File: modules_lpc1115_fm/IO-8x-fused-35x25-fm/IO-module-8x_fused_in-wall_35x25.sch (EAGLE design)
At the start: 82 parts, among them IC1 LPC1115, IC2 ATAES132A-SHEQ-T, Q2 ASFL, U1 EEPROM, X3 MICROMATCH-10

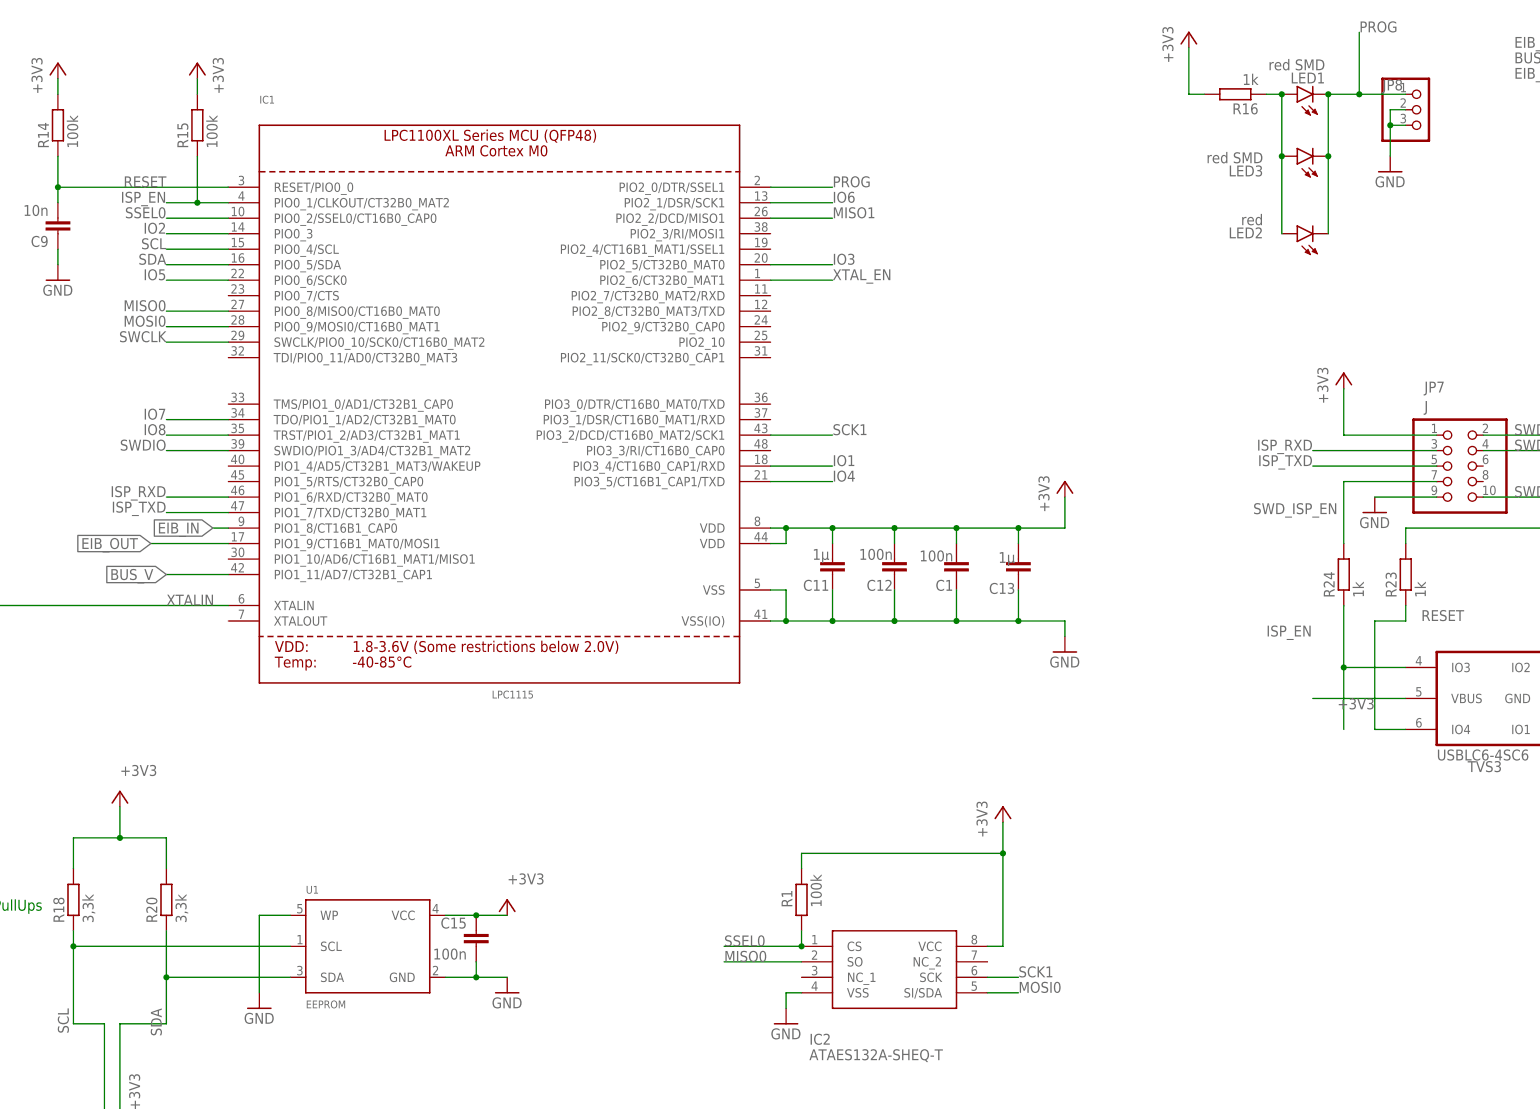
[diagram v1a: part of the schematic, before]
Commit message: [IOmodule8xUP] fixed errors with SPI routing
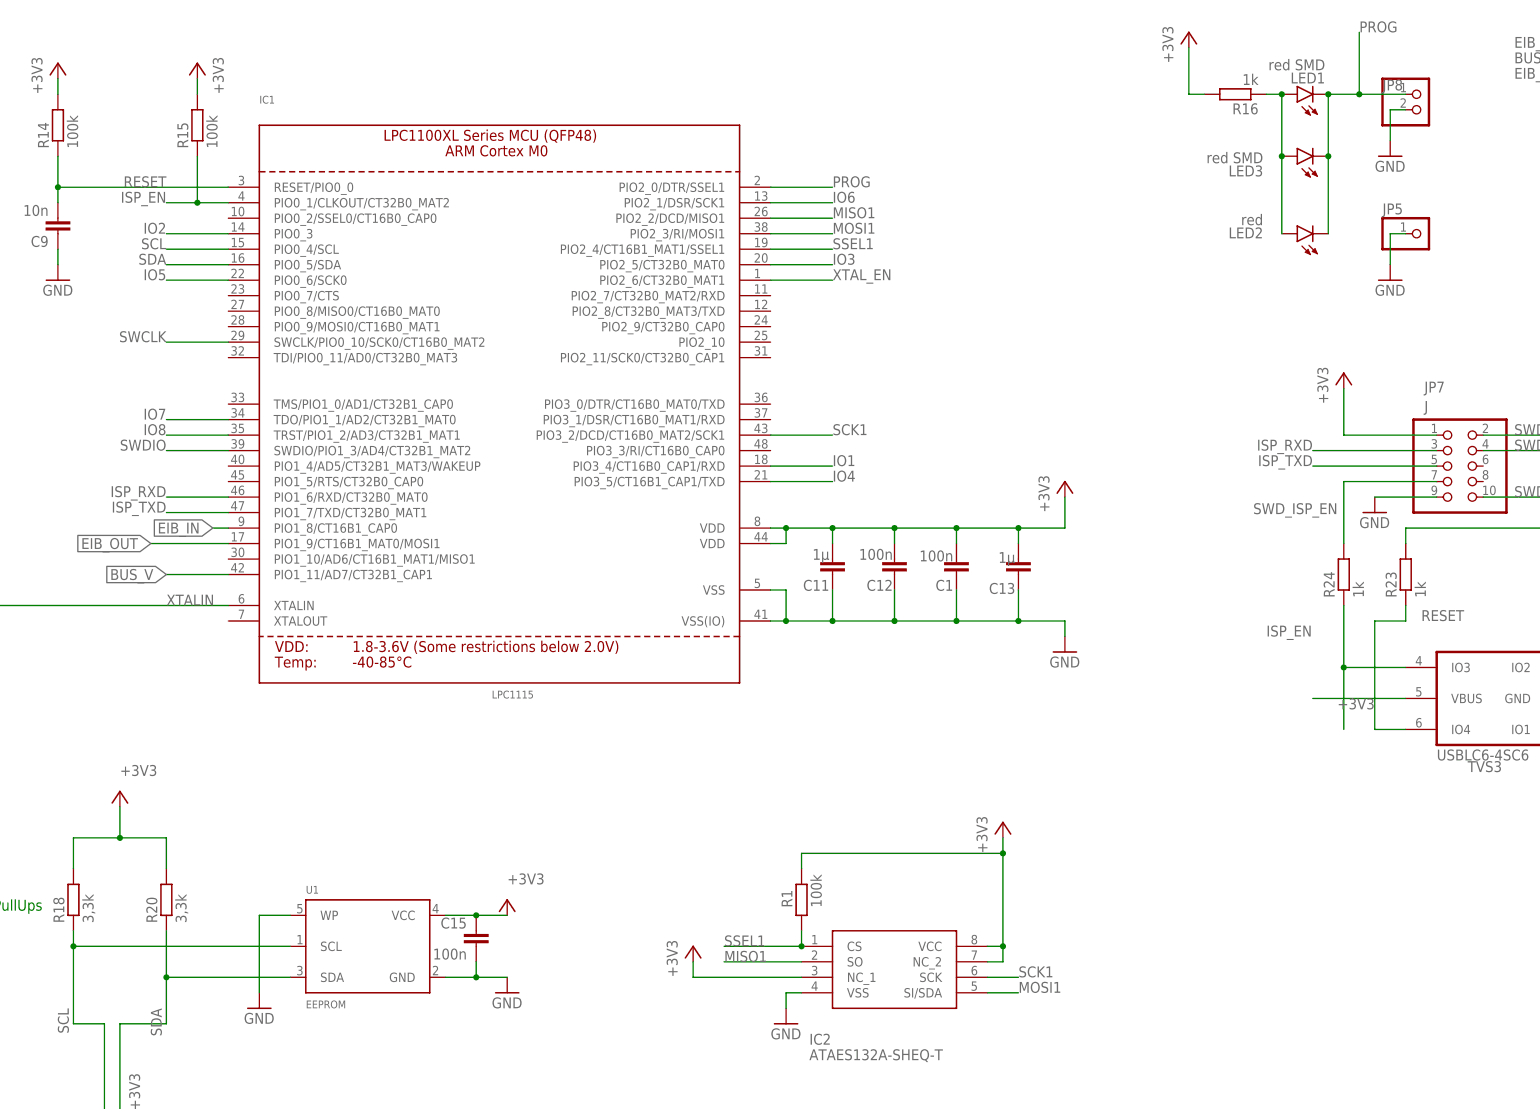
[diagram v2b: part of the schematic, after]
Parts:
- added JP5: (no value), pinhead_dmx:PINHD-1X1
- JP8: device pinhead_dmx:PINHD-1X3 -> pinhead_dmx:PINHD-1X2
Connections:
- removed net MISO0: IC1.PIO0_8/MISO0/CT16B0_MAT0, IC2.SO
- removed net MOSI0: IC1.PIO0_9/MOSI0/CT16B0_MAT1, IC2.SI/SDA
- removed net SSEL0: IC1.PIO0_2/SSEL0/CT16B0_CAP0, IC2.CS, R1.1
- new net MOSI1: IC1.PIO2_3/RI/MOSI1, IC2.SI/SDA
- new net SSEL1: IC1.PIO2_4/CT16B1_MAT1/SSEL1, IC2.CS, R1.1
- net +3V3: now also IC2.NC_1, IC2.NC_2
- net GND: now also JP5.1; no longer JP8.3
- net MISO1: now also IC2.SO
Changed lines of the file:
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@@
 </part>
 <part name="P+4" library="supply1" deviceset="+3V3" device=""/>
-<part name="JP8" library="pinhead_dmx" deviceset="PINHD-1X3" device="" package3d_urn="urn:adsk.eagle:package:22458/2"/>
+<part name="JP8" library="pinhead_dmx" deviceset="PINHD-1X2" device="" package3d_urn="urn:adsk.eagle:package:22435/2"/>
 <part name="LED2" library="led" library_urn="urn:adsk.eagle:library:259" deviceset="LED" device="3MM" package3d_urn="urn:adsk.eagle:package:15797/1" value="red">
 <attribute name="REICHELT" value="SMD-LED 0805 RT"/>
@@
 <part name="R8" library="rcl" library_urn="urn:adsk.eagle:library:334" deviceset="R-EU_" device="R0805" package3d_urn="urn:adsk.eagle:package:23553/2" value="100R"/>
 <part name="R9" library="rcl" library_urn="urn:adsk.eagle:library:334" deviceset="R-EU_" device="R0805" package3d_urn="urn:adsk.eagle:package:23553/2" value="100R"/>
+<part name="JP5" library="pinhead_dmx" deviceset="PINHD-1X1" device="" package3d_urn="urn:adsk.eagle:package:22485/2"/>
+<part name="GND4" library="supply1" deviceset="GND" device=""/>
+<part name="P+9" library="supply1" deviceset="+3V3" device=""/>
 </parts>
 <sheets>
@@
 <attribute name="VALUE" x="472.44" y="193.04" size="1.778" layer="96" rot="R90"/>
 </instance>
-<instance part="JP8" gate="A" x="513.08" y="185.42" smashed="yes">
+<instance part="JP8" gate="G$1" x="513.08" y="185.42" smashed="yes">
 <attribute name="NAME" x="506.73" y="188.595" size="1.778" layer="95"/>
 <attribute name="VALUE" x="506.73" y="180.34" size="1.778" layer="96"/>
@@
 <attribute name="VALUE" x="272.796" y="93.599" size="1.778" layer="96" rot="R180"/>
 </instance>
-<instance part="GND12" gate="1" x="508" y="175.26" smashed="yes">
-<attribute name="VALUE" x="505.46" y="172.72" size="1.778" layer="96"/>
+<instance part="GND12" gate="1" x="508" y="177.8" smashed="yes">
+<attribute name="VALUE" x="505.46" y="175.26" size="1.778" layer="96"/>
 </instance>
 <instance part="TVS3" gate="G$1" x="525.78" y="88.9" smashed="yes" rot="R180">
@@
 <attribute name="VALUE" x="412.75" y="30.48" size="1.778" layer="96" align="center-left"/>
 </instance>
-<instance part="P+7" gate="G$1" x="444.5" y="71.12" smashed="yes">
-<attribute name="VALUE" x="441.96" y="66.04" size="1.778" layer="96" rot="R90"/>
+<instance part="P+7" gate="G$1" x="444.5" y="68.58" smashed="yes">
+<attribute name="VALUE" x="441.96" y="63.5" size="1.778" layer="96" rot="R90"/>
 </instance>
 <instance part="GND2" gate="1" x="408.94" y="35.56" smashed="yes">
@@
 <attribute name="NAME" x="207.01" y="164.0586" size="1.778" layer="91"/>
 <attribute name="VALUE" x="207.01" y="159.258" size="1.778" layer="91"/>
+</instance>
+<instance part="JP5" gate="G$1" x="513.08" y="165.1" smashed="yes">
+<attribute name="NAME" x="506.73" y="168.275" size="1.778" layer="95"/>
+<attribute name="VALUE" x="506.73" y="160.02" size="1.778" layer="96"/>
+</instance>
+<instance part="GND4" gate="1" x="508" y="157.48" smashed="yes">
+<attribute name="VALUE" x="505.46" y="154.94" size="1.778" layer="96"/>
+</instance>
+<instance part="P+9" gate="G$1" x="393.7" y="48.26" smashed="yes">
+<attribute name="VALUE" x="391.16" y="43.18" size="1.778" layer="96" rot="R90"/>
 </instance>
 </instances>
@@
 </segment>
 <segment>
-<pinref part="JP8" gate="A" pin="2"/>
+<pinref part="JP8" gate="G$1" pin="2"/>
 <wire x1="510.54" y1="185.42" x2="508" y2="185.42" width="0.1524" layer="91"/>
-<wire x1="508" y1="185.42" x2="508" y2="182.88" width="0.1524" layer="91"/>
-<pinref part="JP8" gate="A" pin="3"/>
-<wire x1="508" y1="182.88" x2="510.54" y2="182.88" width="0.1524" layer="91"/>
 <pinref part="GND12" gate="1" pin="GND"/>
-<wire x1="508" y1="182.88" x2="508" y2="177.8" width="0.1524" layer="91"/>
-<junction x="508" y="182.88"/>
+<wire x1="508" y1="185.42" x2="508" y2="180.34" width="0.1524" layer="91"/>
 </segment>
 <segment>
@@
 <wire x1="304.8" y1="15.24" x2="304.8" y2="5.08" width="0.1524" layer="91"/>
 <pinref part="JP1" gate="G$1" pin="1"/>
+</segment>
+<segment>
+<pinref part="JP5" gate="G$1" pin="1"/>
+<pinref part="GND4" gate="1" pin="GND"/>
+<wire x1="510.54" y1="165.1" x2="508" y2="165.1" width="0.1524" layer="91"/>
+<wire x1="508" y1="165.1" x2="508" y2="160.02" width="0.1524" layer="91"/>
 </segment>
 </net>
@@
 </segment>
 </net>
-<net name="MOSI0" class="0">
-<segment>
-<pinref part="IC1" gate="G$1" pin="PIO0_9/MOSI0/CT16B0_MAT1"/>
-<wire x1="307.34" y1="149.86" x2="317.5" y2="149.86" width="0.1524" layer="91"/>
-<label x="307.34" y="149.86" size="1.778" layer="95" rot="MR0"/>
-</segment>
-<segment>
-<pinref part="IC2" gate="G$1" pin="SI/SDA"/>
-<wire x1="441.96" y1="40.64" x2="447.04" y2="40.64" width="0.1524" layer="91"/>
-<label x="447.04" y="40.64" size="1.778" layer="95"/>
-</segment>
-</net>
 <net name="SWDIO" class="0">
 <segment>
@@
 <wire x1="551.18" y1="93.98" x2="538.48" y2="93.98" width="0.1524" layer="91"/>
 <junction x="551.18" y="93.98"/>
-</segment>
-</net>
-<net name="MISO0" class="0">
-<segment>
-<pinref part="IC1" gate="G$1" pin="PIO0_8/MISO0/CT16B0_MAT0"/>
-<wire x1="307.34" y1="152.4" x2="317.5" y2="152.4" width="0.1524" layer="91"/>
-<label x="307.34" y="152.4" size="1.778" layer="95" rot="MR0"/>
-</segment>
-<segment>
-<pinref part="IC2" gate="G$1" pin="SO"/>
-<label x="398.78" y="45.72" size="1.778" layer="95"/>
-<wire x1="411.48" y1="45.72" x2="398.78" y2="45.72" width="0.1524" layer="91"/>
 </segment>
 </net>
@@
 <label x="502.92" y="198.12" size="1.778" layer="95"/>
 <junction x="502.92" y="187.96"/>
-<pinref part="JP8" gate="A" pin="1"/>
+<pinref part="JP8" gate="G$1" pin="1"/>
 <pinref part="LED2" gate="G$1" pin="C"/>
 <wire x1="497.84" y1="165.1" x2="497.84" y2="177.8" width="0.1524" layer="91"/>
@@
 <wire x1="444.5" y1="48.26" x2="444.5" y2="63.5" width="0.1524" layer="91"/>
 <pinref part="R1" gate="G$1" pin="2"/>
-<wire x1="444.5" y1="63.5" x2="444.5" y2="68.58" width="0.1524" layer="91"/>
+<wire x1="444.5" y1="63.5" x2="444.5" y2="66.04" width="0.1524" layer="91"/>
 <wire x1="411.48" y1="60.96" x2="411.48" y2="63.5" width="0.1524" layer="91"/>
 <wire x1="411.48" y1="63.5" x2="444.5" y2="63.5" width="0.1524" layer="91"/>
 <junction x="444.5" y="63.5"/>
+<pinref part="IC2" gate="G$1" pin="NC_2"/>
+<wire x1="441.96" y1="45.72" x2="444.5" y2="45.72" width="0.1524" layer="91"/>
+<wire x1="444.5" y1="45.72" x2="444.5" y2="48.26" width="0.1524" layer="91"/>
+<junction x="444.5" y="48.26"/>
 </segment>
 <segment>
@@
 <pinref part="JP1" gate="G$1" pin="2"/>
 <wire x1="302.26" y1="17.78" x2="302.26" y2="15.24" width="0.1524" layer="91"/>
+</segment>
+<segment>
+<pinref part="IC2" gate="G$1" pin="NC_1"/>
+<wire x1="411.48" y1="43.18" x2="393.7" y2="43.18" width="0.1524" layer="91"/>
+<pinref part="P+9" gate="G$1" pin="+3V3"/>
+<wire x1="393.7" y1="45.72" x2="393.7" y2="43.18" width="0.1524" layer="91"/>
 </segment>
 </net>
@@
 <label x="416.56" y="167.64" size="1.778" layer="95"/>
 </segment>
+<segment>
+<pinref part="IC2" gate="G$1" pin="SO"/>
+<label x="398.78" y="45.72" size="1.778" layer="95"/>
+<wire x1="411.48" y1="45.72" x2="398.78" y2="45.72" width="0.1524" layer="91"/>
+</segment>
 </net>
 <net name="IN1" class="0">
@@
 <wire x1="441.96" y1="43.18" x2="447.04" y2="43.18" width="0.1524" layer="91"/>
 <label x="447.04" y="43.18" size="1.778" layer="95"/>
-</segment>
-</net>
-<net name="SSEL0" class="0">
-<segment>
-<pinref part="IC2" gate="G$1" pin="CS"/>
-<pinref part="R1" gate="G$1" pin="1"/>
-<wire x1="411.48" y1="48.26" x2="411.48" y2="50.8" width="0.1524" layer="91"/>
-<junction x="411.48" y="48.26"/>
-<wire x1="411.48" y1="48.26" x2="398.78" y2="48.26" width="0.1524" layer="91"/>
-<label x="398.78" y="48.26" size="1.778" layer="95"/>
-</segment>
-<segment>
-<pinref part="IC1" gate="G$1" pin="PIO0_2/SSEL0/CT16B0_CAP0"/>
-<wire x1="317.5" y1="167.64" x2="307.34" y2="167.64" width="0.1524" layer="91"/>
-<label x="307.34" y="167.64" size="1.778" layer="95" align="bottom-right"/>
 </segment>
 </net>
@@
 <label x="187.96" y="139.7" size="1.778" layer="95"/>
 <pinref part="R8" gate="G$1" pin="1"/>
+</segment>
+</net>
+<net name="MOSI1" class="0">
+<segment>
+<pinref part="IC1" gate="G$1" pin="PIO2_3/RI/MOSI1"/>
+<wire x1="406.4" y1="165.1" x2="416.56" y2="165.1" width="0.1524" layer="91"/>
+<label x="416.56" y="165.1" size="1.778" layer="95"/>
+</segment>
+<segment>
+<pinref part="IC2" gate="G$1" pin="SI/SDA"/>
+<wire x1="441.96" y1="40.64" x2="447.04" y2="40.64" width="0.1524" layer="91"/>
+<label x="447.04" y="40.64" size="1.778" layer="95"/>
+</segment>
+</net>
+<net name="SSEL1" class="0">
+<segment>
+<pinref part="IC1" gate="G$1" pin="PIO2_4/CT16B1_MAT1/SSEL1"/>
+<wire x1="406.4" y1="162.56" x2="416.56" y2="162.56" width="0.1524" layer="91"/>
+<label x="416.56" y="162.56" size="1.778" layer="95"/>
+</segment>
+<segment>
+<pinref part="IC2" gate="G$1" pin="CS"/>
+<pinref part="R1" gate="G$1" pin="1"/>
+<wire x1="411.48" y1="48.26" x2="411.48" y2="50.8" width="0.1524" layer="91"/>
+<junction x="411.48" y="48.26"/>
+<wire x1="411.48" y1="48.26" x2="398.78" y2="48.26" width="0.1524" layer="91"/>
+<label x="398.78" y="48.26" size="1.778" layer="95"/>
 </segment>
 </net>
@@
 for full support of SPICE simulation.
 </note>
-<note version="9.0" severity="warning">
-Since Version 9.0, EAGLE supports the align property for labels.
-Labels in schematic will not be understood with this version. Update EAGLE to the latest version
-for full support of labels.
-</note>
 </compatibility>

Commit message: [IOmodule8xUP] several errors fixed - see detailed message
switch to MISO1/MOSI1 with SCK1
changed order of TVS3 and SWD components 
fixed unconnected +3V3 pin at SWD header
fixed width of THT holes for prog button
connected pin 3 and 7 of IC2 to +3V3 so that also a flash IC could beused
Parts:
- removed JP5: (no value), pinhead_dmx:PINHD-1X1
- added PRGBTN: (no value), pinhead_dmx:PINHD-1X1
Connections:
- net GND: now also PRGBTN.1; no longer JP5.1
- net ISP_EN: no longer TVS3.IO3
- net RESET: now also R23.2; no longer R23.1, TVS3.IO4
- net SWCLK: no longer TVS3.IO1
- net SWDIO: no longer TVS3.IO2
- net SWD_ISP_EN: now also TVS3.IO3
- net SWD_RESET: now also R23.1, TVS3.IO4; no longer R23.2
- net SWD_SWCLK: now also JP7.2, R19.2, TVS3.IO2; no longer JP7.4, R17.2
- net SWD_SWDIO: now also JP7.4, R17.2, TVS3.IO1; no longer JP7.2, R19.2
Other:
- moved on the sheet: C20, D31, D32, D35, D36, D37, D38, D41, D42, F17, F18, F19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
